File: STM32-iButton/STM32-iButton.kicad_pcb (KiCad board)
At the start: 2 copper layers, 49.7 x 19.5 mm, 8 parts, among them J1 Conn_SWD, J2 Conn_SWD, P1 USB_C_2.0, SW1 Button_user, SW2 Button_user, SW3 Button_user, U1 STM32L052C8Tx, U2 AMS1117-3.3

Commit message: updated
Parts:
- added C1: 10uF, Capacitor_SMD:C_0603_1608Metric_Pad1.08x0.95mm_HandSolder, F.Cu at (69.0, 31.5)
- added C2: 10uF, Capacitor_SMD:C_0603_1608Metric_Pad1.08x0.95mm_HandSolder, F.Cu at (69.0, 29.5)
- added R1: 1.5k, Resistor_SMD:R_0603_1608Metric_Pad0.98x0.95mm_HandSolder, F.Cu at (74.6, 31.5)
- added R2: 10k, Resistor_SMD:R_0603_1608Metric_Pad0.98x0.95mm_HandSolder, F.Cu at (88.4, 31.5)
- P1: footprint Connector_USB:USB_C_Plug_JAE_DX07P024AJ1 -> wyw-conn:USB_C_Male
- moved P1 6.98 mm to (81.9, 25.6)
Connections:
- SW1 pad 1: unconnected-(SW1-Pad1) -> /Btn1
- SW1 pad 2: unconnected-(SW1-Pad2) -> GND
- SW2 pad 1: unconnected-(SW2-Pad1) -> /Btn2
- SW2 pad 2: unconnected-(SW2-Pad2) -> GND
- SW3 pad 1: unconnected-(SW3-Pad1) -> /Btn3
- SW3 pad 2: unconnected-(SW3-Pad2) -> GND
- U1 pad 2: unconnected-(U1-PC13-Pad2) -> /Btn1
- U1 pad 3: unconnected-(U1-PC14-Pad3) -> /Btn2
- U1 pad 4: unconnected-(U1-PC15-Pad4) -> /Btn3
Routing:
- net +3.3V: track 0.00 -> 97.4 mm, vias 0 -> 7
- net /SWDIO: track 0.00 -> 52.6 mm, vias 0 -> 1
- net /Boot: track 0.00 -> 49.1 mm, vias 0 -> 3
- net /SWCLK: track 0.00 -> 43.8 mm, vias 0 -> 1
- net /Btn3: track 0.00 -> 36.5 mm, vias 0 -> 1
- net /Btn2: track 0.00 -> 25.0 mm, vias 0 -> 1
- net Net-(U2-VI): track 0.00 -> 23.6 mm, vias 0 -> 1
- net /D-: track 0.00 -> 23.0 mm, vias 0 -> 1
- net GND: track 0.00 -> 21.0 mm, vias 0 -> 30
- net /D+: track 0.00 -> 20.6 mm, vias 0 -> 1
- net /Btn1: track 0.00 -> 12.0 mm, vias 0 -> 1
- added copper zone on F.Cu, net GND
- removed copper zone on F.Cu, net +3.3V
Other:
- board size 49.7 x 19.5 mm -> 49.7 x 18 mm

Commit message: add fab release
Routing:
- net Net-(U2-VI): track 23.6 -> 27.3 mm, vias 1 -> 2
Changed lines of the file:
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@@
 			(outputformat 1)
 			(mirror no)
-			(drillshape 1)
+			(drillshape 0)
 			(scaleselection 1)
-			(outputdirectory "")
+			(outputdirectory "Fab/")
 		)
 	)
@@
 		(tags "resistor handsolder")
 		(property "Reference" "R1"
-			(at 0 -1.43 360)
+			(at 0 -1.43 0)
 			(layer "F.Fab")
 			(effects
@@
 		)
 		(property "Value" "1.5k"
-			(at 0 1.43 360)
+			(at 0 1.43 0)
 			(layer "F.Fab")
 			(effects
@@
 		)
 		(fp_text user "${REFERENCE}"
-			(at 0 0 360)
+			(at 0 0 0)
 			(layer "F.Fab")
 			(effects
@@
 	)
 	(segment
+		(start 83.15 29)
+		(end 83.15 29.95)
+		(width 0.2)
+		(layer "F.Cu")
+		(net 41)
+	)
+	(segment
+		(start 83.15 29.95)
+		(end 82.675 30.425)
+		(width 0.2)
+		(layer "F.Cu")
+		(net 41)
+	)
+	(segment
 		(start 69.1375 30.5)
 		(end 79.75 30.5)
@@
 		(net 41)
 	)
+	(via
+		(at 82.675 30.425)
+		(size 0.6)
+		(drill 0.3)
+		(layers "F.Cu" "B.Cu")
+		(net 41)
+	)
 	(segment
 		(start 82.6 30.5)
@@
 	(segment
 		(start 83.15 29.95)
-		(end 82.6 30.5)
+		(end 82.675 30.425)
+		(width 0.2)
+		(layer "B.Cu")
+		(net 41)
+	)
+	(segment
+		(start 80.65 29)
+		(end 80.65 29.95)
+		(width 0.2)
+		(layer "B.Cu")
+		(net 41)
+	)
+	(segment
+		(start 80.1 30.5)
+		(end 79.75 30.5)
 		(width 0.2)
 		(layer "B.Cu")
@@
 		(width 0.2)
 		(layer "B.Cu")
+		(net 41)
+	)
+	(segment
+		(start 80.65 29.95)
+		(end 80.1 30.5)
+		(width 0.2)
+		(layer "B.Cu")
+		(net 41)
+	)
+	(segment
+		(start 82.675 30.425)
+		(end 82.6 30.5)
+		(width 0.2)
+		(layer "B.Cu")

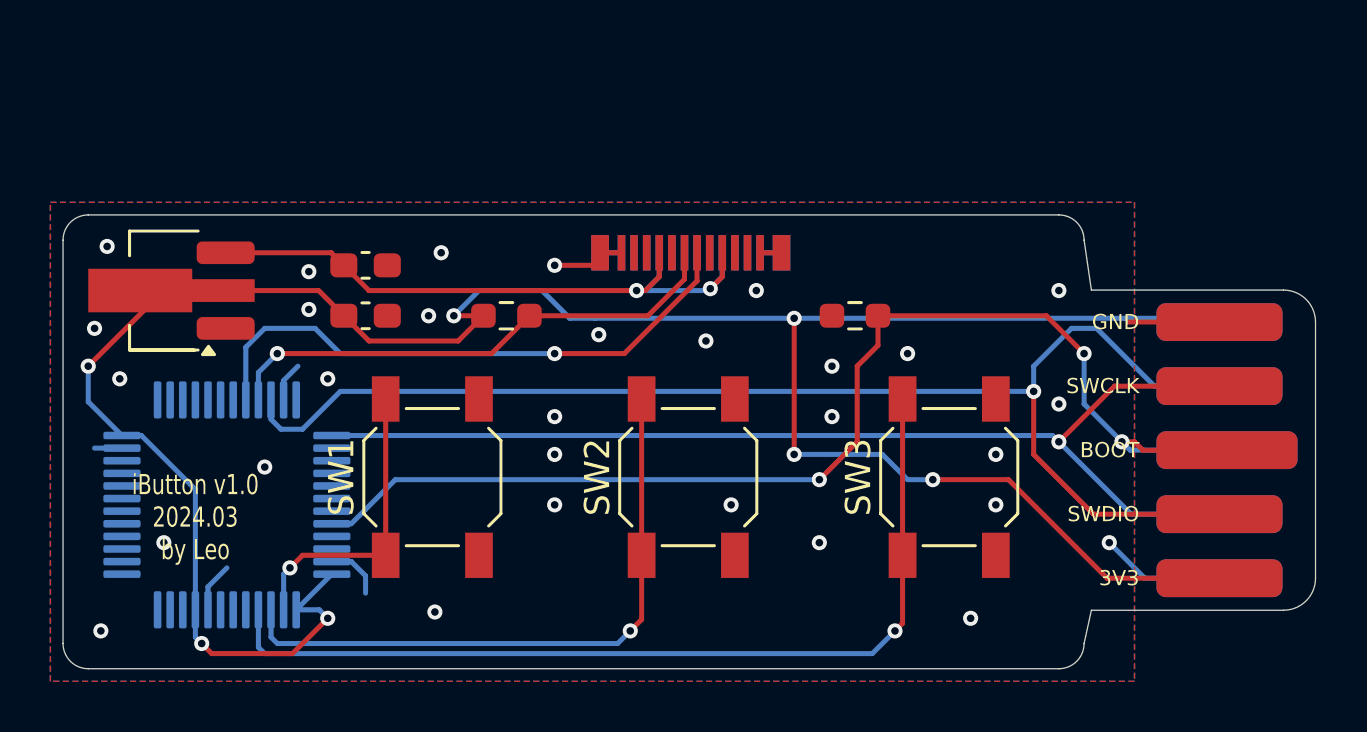
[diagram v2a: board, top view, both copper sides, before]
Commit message: critical fix: 5V power
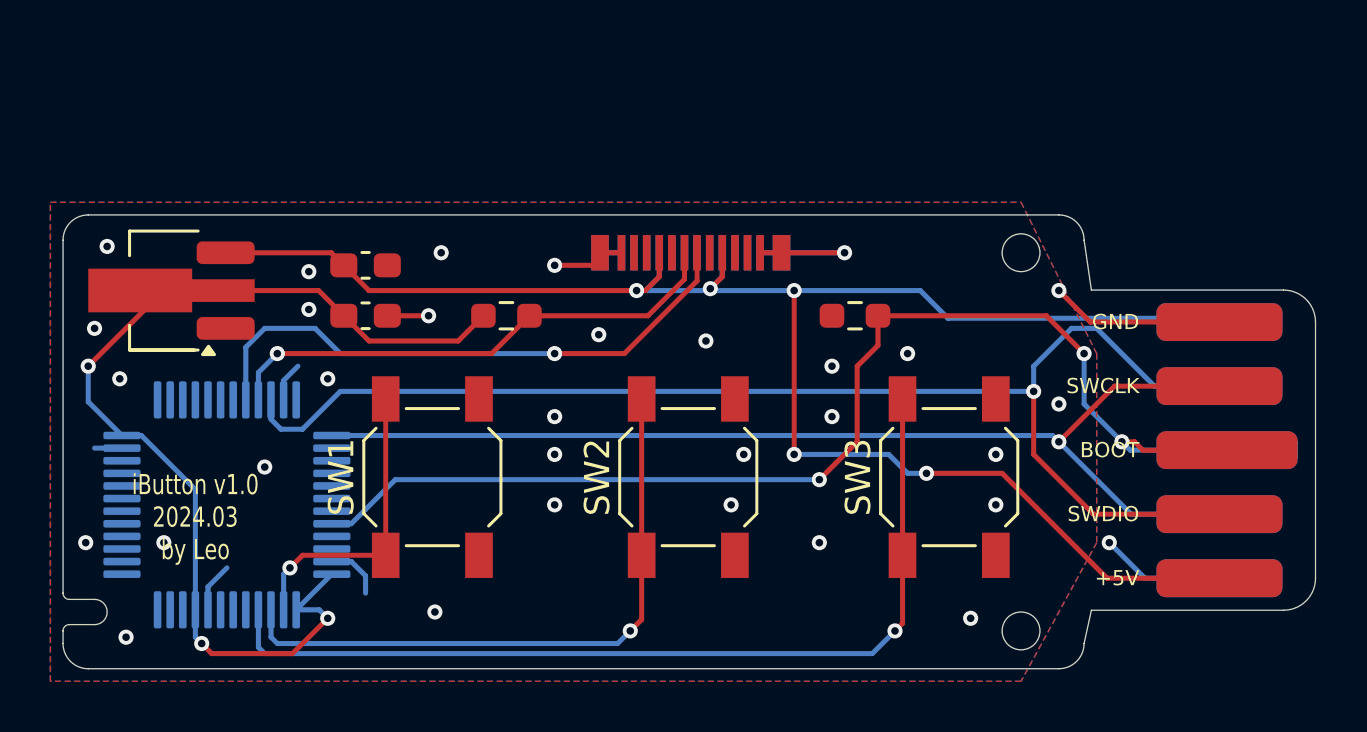
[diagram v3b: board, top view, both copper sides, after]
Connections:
- C2 pad 1: Net-(U2-VI) -> +5V
- J1 pad 1: +3.3V -> +5V
- J2 pad 1: +3.3V -> +5V
- P1 pad A4: Net-(U2-VI) -> +5V
- P1 pad A9: Net-(U2-VI) -> +5V
- P1 pad B4: Net-(U2-VI) -> +5V
- P1 pad B9: Net-(U2-VI) -> +5V
- U2 pad 3: Net-(U2-VI) -> +5V
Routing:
- net +5V: track 0.00 -> 73.4 mm, vias 0 -> 5
- net +3.3V: track 97.4 -> 40.6 mm, vias 7 -> 3
- net Net-(U2-VI): track 27.3 -> 0.00 mm, vias 2 -> 0
- net GND: track 21.0 -> 30.9 mm, vias 30 -> 32
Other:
- outline, holes or cut-outs redrawn
- board text added: "+5V"
- board text removed: "3V3"

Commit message: added stlink edge 3
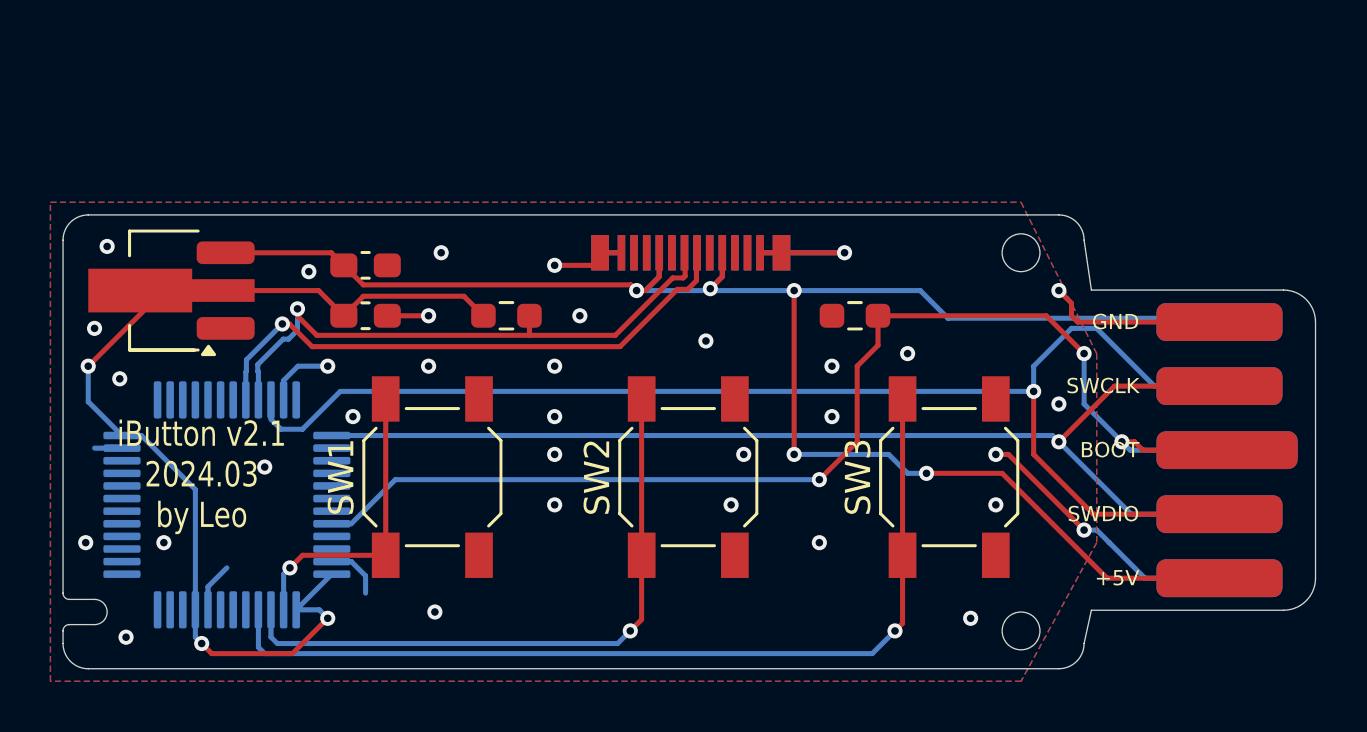
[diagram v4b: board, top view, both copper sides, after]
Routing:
- net GND: track 30.9 -> 38.3 mm, vias 32 -> 34
- net /D+: track 20.6 -> 23.6 mm
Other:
- board text added: "iButton v2.1 2024.03 by Leo"
- board text removed: "iButton v1.0 2024.03 by Leo"
